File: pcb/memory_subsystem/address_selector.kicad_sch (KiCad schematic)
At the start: 12 parts, among them U16 74LS32, U17 74LS139, U18 74LS161, U19 74LS157, U20 74LS161, U21 74LS157

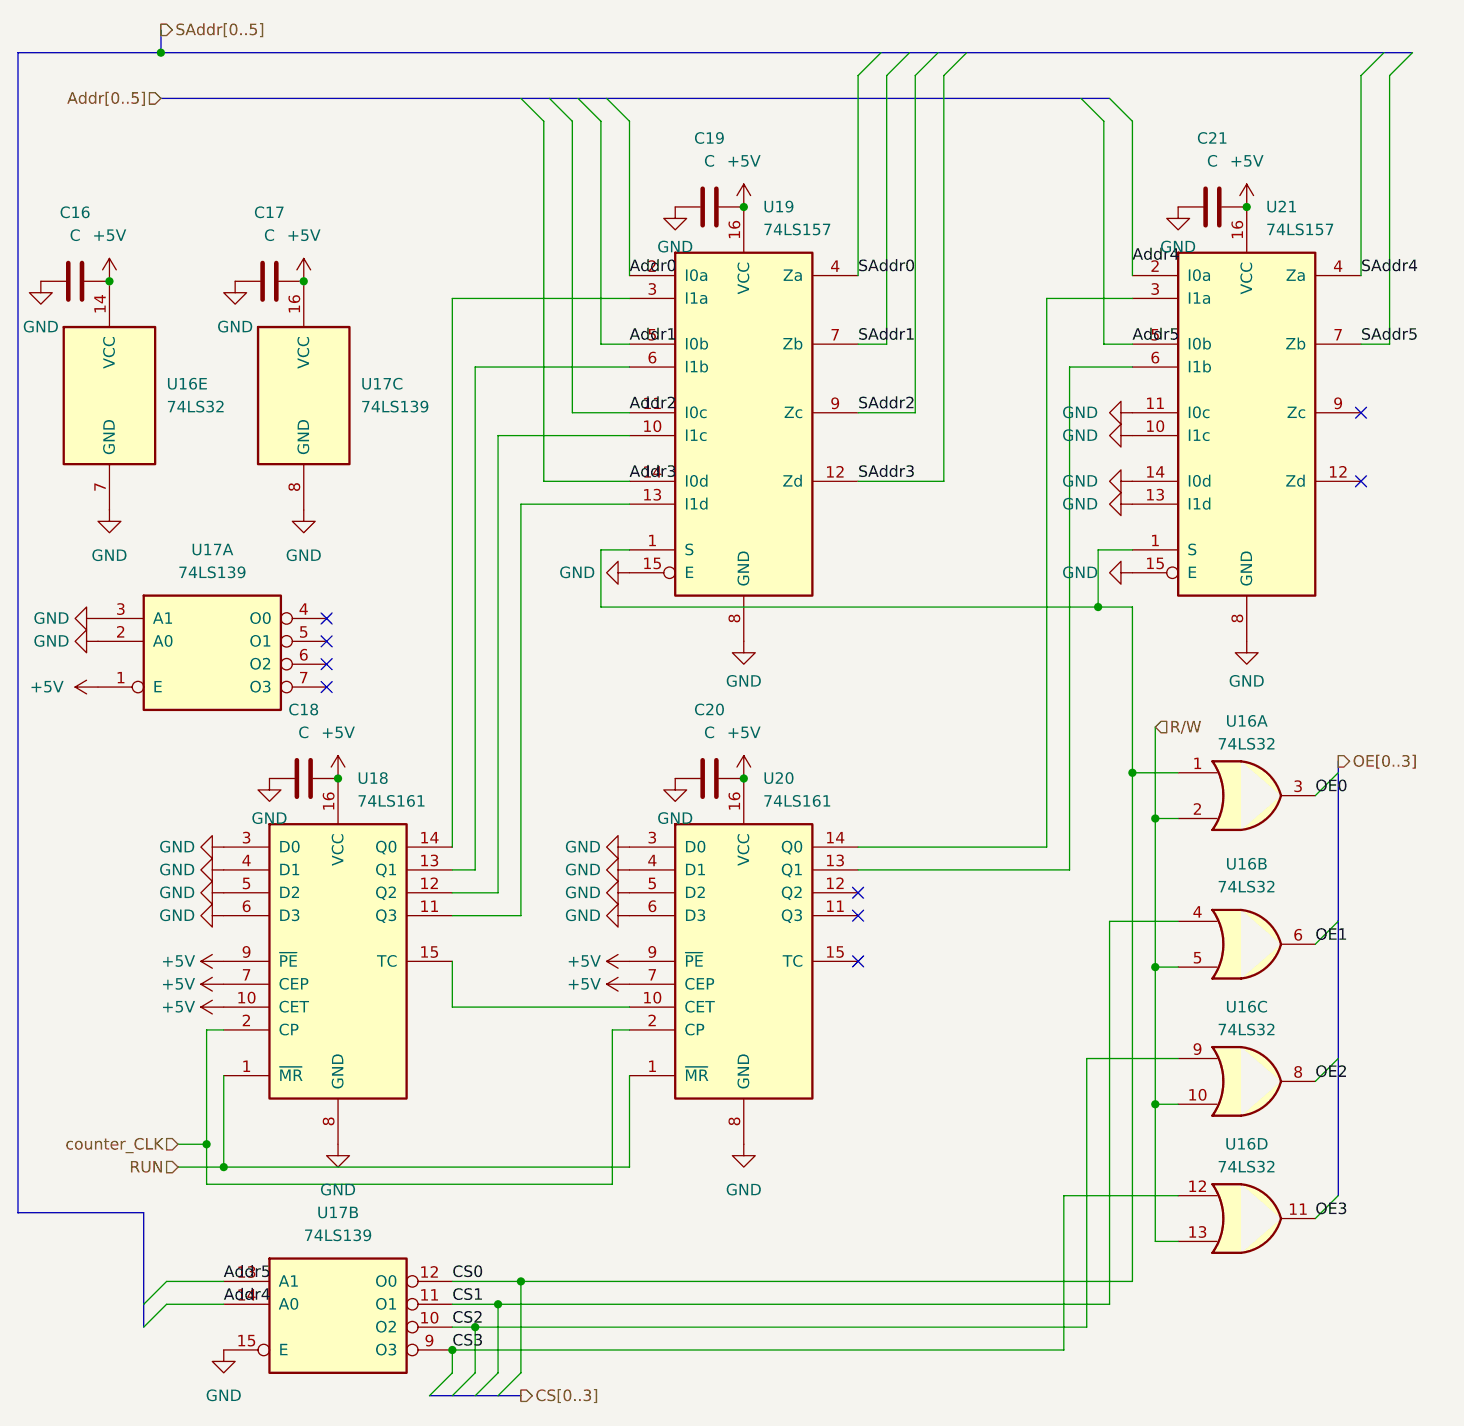
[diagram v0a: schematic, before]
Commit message: Fixed spacing problem: no warnings/erros
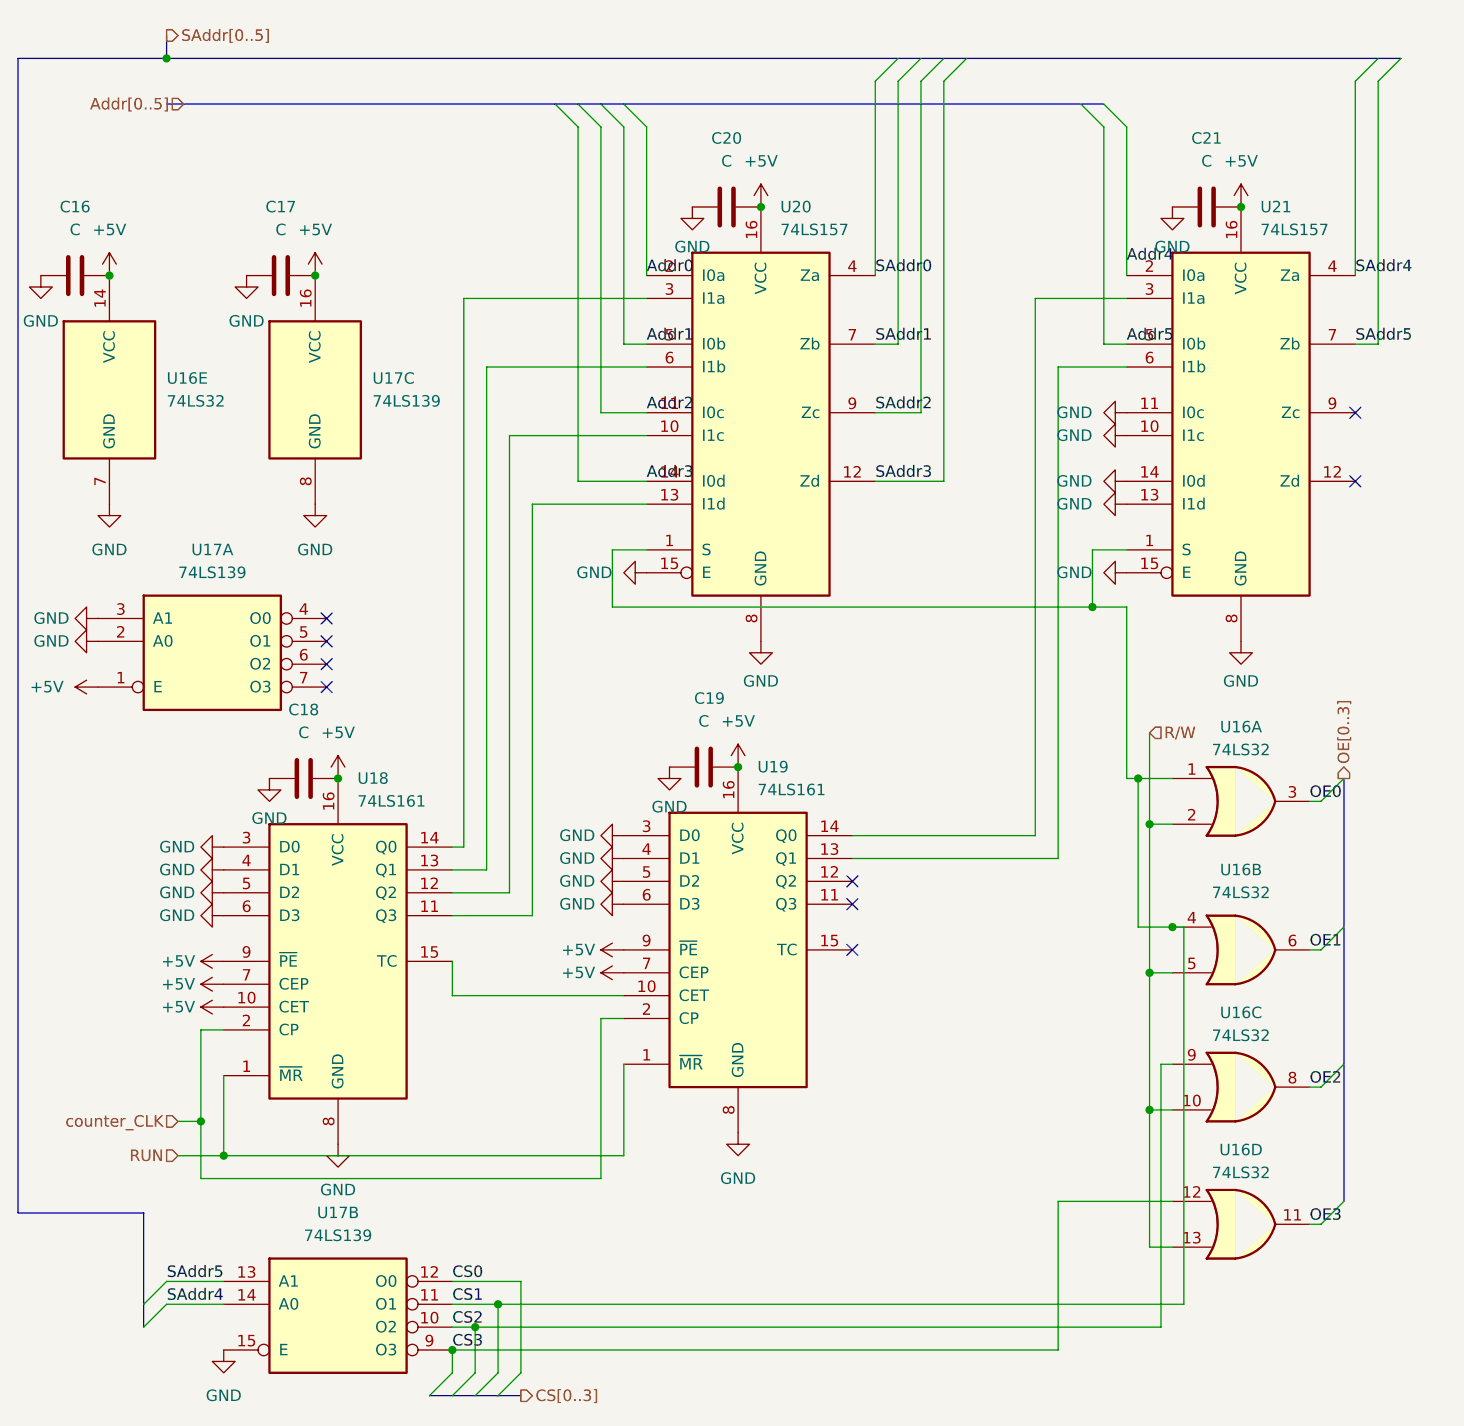
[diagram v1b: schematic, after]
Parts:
- renumbered C20 to C19, C19 to C20, U20 to U19, U19 to U20
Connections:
- net Addr4: no longer U17.14 (A0)
- net Addr5: no longer U17.13 (A1)
- net CS0: no longer U16.1, U20.1 (S), U21.1 (S)
- net CS1: now also U16.1, U20.1 (S), U21.1 (S)
- net SAddr4: now also U17.14 (A0)
- net SAddr5: now also U17.13 (A1)
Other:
- moved on the sheet: C16, C17, C19, C20, C21, U16A, U16B, U16C, U16D, U16E, U17C, U19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

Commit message: Tracks finished
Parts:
- C16, C17: footprint Capacitor_SMD:C_0805_2012Metric -> Capacitor_SMD:C_0805_2012Metric_Pad1.18x1.45mm_HandSolder
- C18, C19, C20, C21: footprint (none) -> Capacitor_SMD:C_0805_2012Metric_Pad1.18x1.45mm_HandSolder
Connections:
- net CS0: now also U16.1
- net CS1: no longer U16.1, U20.1 (S), U21.1 (S)
- net R/W: now also U20.1 (S), U21.1 (S)
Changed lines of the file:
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@@
 	)
 	(junction
-		(at 143.51 99.06)
-		(diameter 0)
-		(color 0 0 0 0)
-	)
-	(junction
-		(at 147.32 115.57)
-		(diameter 0)
-		(color 0 0 0 0)
-	)
-	(junction
 		(at 35.56 19.05)
 		(diameter 0)
@@
 		(color 0 0 0 0)
 	)
+	(junction
+		(at 74.93 154.94)
+		(diameter 0)
+		(color 0 0 0 0)
+	)
 	(no_connect
 		(at 111.76 110.49)
@@
 		)
 	)
+	(wire
+		(pts
+			(xy 147.32 99.06) (xy 143.51 99.06)
+		)
+		(stroke
+			(width 0)
+			(type default)
+		)
+	)
 	(bus
 		(pts
@@
 	(wire
 		(pts
-			(xy 147.32 120.65) (xy 144.78 120.65)
+			(xy 142.24 80.01) (xy 142.24 93.98)
 		)
 		(stroke
@@
 	(wire
 		(pts
-			(xy 86.36 26.67) (xy 86.36 50.8)
+			(xy 147.32 120.65) (xy 144.78 120.65)
 		)
 		(stroke
@@
 	(wire
 		(pts
-			(xy 143.51 99.06) (xy 142.24 99.06)
+			(xy 86.36 26.67) (xy 86.36 50.8)
 		)
 		(stroke
@@
 	(wire
 		(pts
-			(xy 67.31 162.56) (xy 67.31 165.1)
+			(xy 143.51 99.06) (xy 143.51 154.94)
 		)
 		(stroke
@@
 	(wire
 		(pts
-			(xy 36.83 137.16) (xy 39.37 137.16)
+			(xy 67.31 162.56) (xy 67.31 165.1)
 		)
 		(stroke
@@
 		)
 	)
-	(bus
+	(wire
 		(pts
-			(xy 72.39 167.64) (xy 74.93 167.64)
+			(xy 36.83 137.16) (xy 39.37 137.16)
 		)
 		(stroke
@@
 		)
 	)
-	(wire
+	(bus
 		(pts
-			(xy 142.24 99.06) (xy 142.24 80.01)
+			(xy 72.39 167.64) (xy 74.93 167.64)
 		)
 		(stroke
@@
 	(wire
 		(pts
-			(xy 143.51 99.06) (xy 143.51 115.57)
+			(xy 41.91 140.97) (xy 86.36 140.97)
 		)
 		(stroke
@@
 	(wire
 		(pts
-			(xy 41.91 140.97) (xy 86.36 140.97)
+			(xy 67.31 162.56) (xy 134.62 162.56)
 		)
 		(stroke
@@
 	(wire
 		(pts
-			(xy 67.31 162.56) (xy 134.62 162.56)
+			(xy 143.51 154.94) (xy 74.93 154.94)
 		)
 		(stroke
@@
 		)
 	)
-	(wire
-		(pts
-			(xy 147.32 99.06) (xy 143.51 99.06)
-		)
-		(stroke
-			(width 0)
-			(type default)
-		)
-	)
 	(bus
 		(pts
@@
 		)
 	)
-	(wire
+	(bus
 		(pts
-			(xy 147.32 115.57) (xy 143.51 115.57)
+			(xy 19.05 147.32) (xy 19.05 19.05)
 		)
 		(stroke
@@
 		)
 	)
-	(bus
+	(wire
 		(pts
-			(xy 19.05 147.32) (xy 19.05 19.05)
+			(xy 142.24 93.98) (xy 144.78 93.98)
 		)
 		(stroke
@@
 			)
 		)
-		(property "Footprint" ""
+		(property "Footprint" "Capacitor_SMD:C_0805_2012Metric_Pad1.18x1.45mm_HandSolder"
 			(at 54.61 98.0948 0)
 			(hide yes)
@@
 			)
 		)
-		(property "Footprint" ""
+		(property "Footprint" "Capacitor_SMD:C_0805_2012Metric_Pad1.18x1.45mm_HandSolder"
 			(at 154.94 34.5948 0)
 			(hide yes)
@@
 			)
 		)
-		(property "Footprint" ""
+		(property "Footprint" "Capacitor_SMD:C_0805_2012Metric_Pad1.18x1.45mm_HandSolder"
 			(at 99.06 96.8248 0)
 			(hide yes)
@@
 			)
 		)
-		(property "Footprint" "Capacitor_SMD:C_0805_2012Metric"
+		(property "Footprint" "Capacitor_SMD:C_0805_2012Metric_Pad1.18x1.45mm_HandSolder"
 			(at 29.21 42.2148 0)
 			(hide yes)
@@
 			)
 		)
-		(property "Footprint" ""
+		(property "Footprint" "Capacitor_SMD:C_0805_2012Metric_Pad1.18x1.45mm_HandSolder"
 			(at 101.6 34.5948 0)
 			(hide yes)
@@
 			)
 		)
-		(property "Footprint" "Capacitor_SMD:C_0805_2012Metric"
+		(property "Footprint" "Capacitor_SMD:C_0805_2012Metric_Pad1.18x1.45mm_HandSolder"
 			(at 44.45 44.1452 0)
 			(hide yes)
